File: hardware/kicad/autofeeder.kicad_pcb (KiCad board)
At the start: 4 copper layers, 56 x 54 mm, 44 parts, among them J1 JST_XH_B2B-XH-A_1x02_P2.50mm_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, J3 USB_C_Receptacle_HRO_TYPE-C-3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, J4 PinHeader_1x04_P2.54mm_Vertic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, SW1_POWER1 SW_Push_1P1T_NO_CK_KMR2, SW2_TIMER1 SW_Push_1P1T_NO_CK_KMR2, SW3_MANUAL1 SW_Push_1P1T_NO_CK_KMR2, SW4_SETTINGS1 SW_Push_1P1T_NO_CK_KMR2, SW5_UP1 SW_Push_1P1T_NO_CK_KMR2, SW6_DOWN1 SW_Push_1P1T_NO_CK_KMR2, U1 ESP32_C6_Zero, U2 SOIC-8_3.9x4.9mm_P1.27mm, U3 SOT-23-6_Handsoldering, U4 WSON-10-1EP_2.5x2.5mm_P0.5mm_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, U6 SOIC-8_3.9x4.9mm_P1.27mm, U8 SOT-23-6_Handsoldering

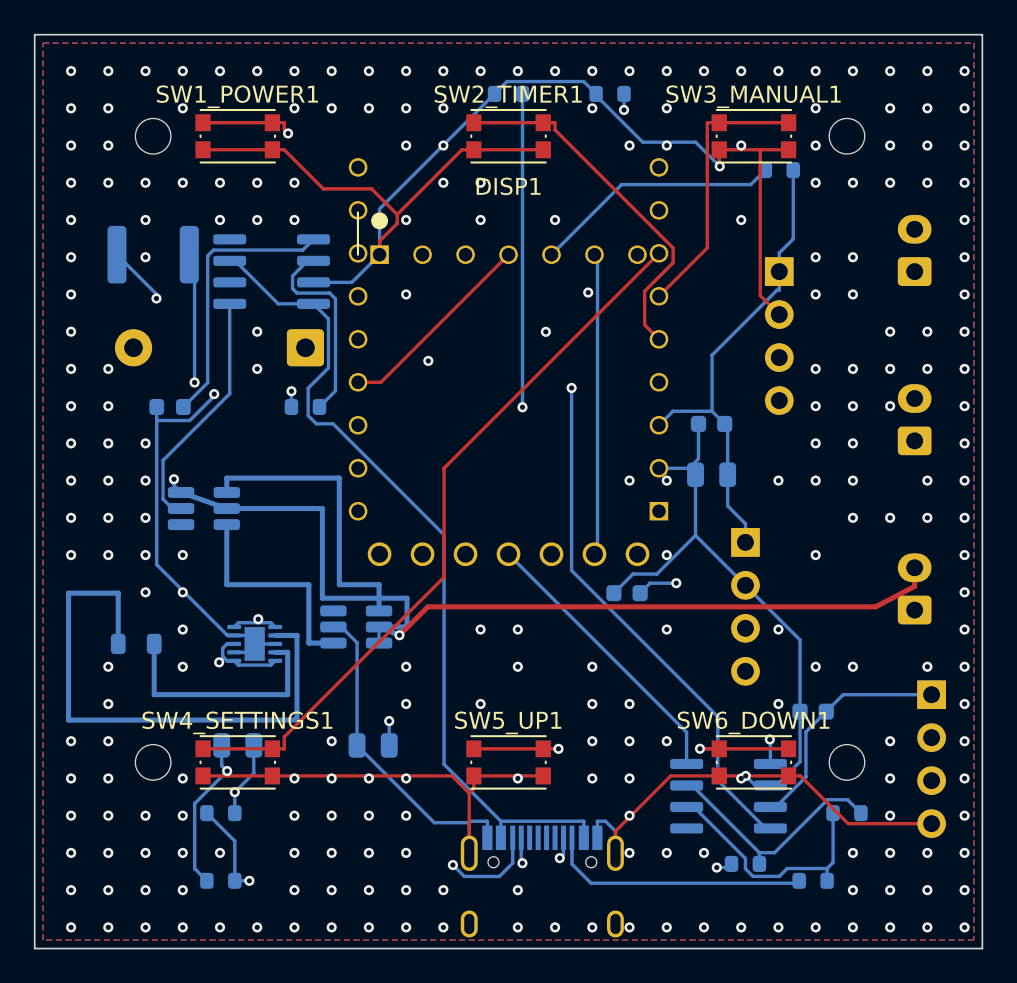
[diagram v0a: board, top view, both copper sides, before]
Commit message: Fix three real shorts in BATT_N pre-routes (battery short + gate crossing)
Commit 04d4fbc shipped 3 DRC error-level violations mislabeled as "marginal
clearance". They were real shorts, all in _pre_route_batt_n():

  1. BATT_N F.Cu track grazed J1 pad 1 (BATT_P) -> dead short across the battery.
  2. OD_GATE (x=20.35 vert) and BATT_N (y=33.3 horiz) crossed on B.Cu at
     (20.35,33.3) -> gate/BATT_N short.
  3. Solder-mask bridge at the same spot as #1.

Fixes:
  - F.Cu J1 exit rerouted left at y=31.5 then down at x=49.69 (left of pad 1's
    x=51 edge), so it never approaches BATT_P.
  - B.Cu U3->U8-2 chain keeps the high y=33.3 path but hops OVER the OD_GATE
    vertical on F.Cu (x19.5->21.2) with two through-vias. Keeping BATT_N high
    preserves the GND pour flow through the U8 inter-column gap that feeds the
    U8-5 GND pocket (a first attempt routing BATT_N down that gap isolated the
    pocket into an unconnected GND island).

Verified (kicad-cli pcb drc --severity-all --schematic-parity): 0 unconnected,
0 error-level violations, B.Cu GND is a single connected plane. Remaining: 11
cosmetic silk warnings + 95 pre-existing schematic-parity items. Fab outputs
(gerbers, drill, DRC) regenerated.

Co-Authored-By: Claude Opus 4.8 <noreply@anthropic.com>
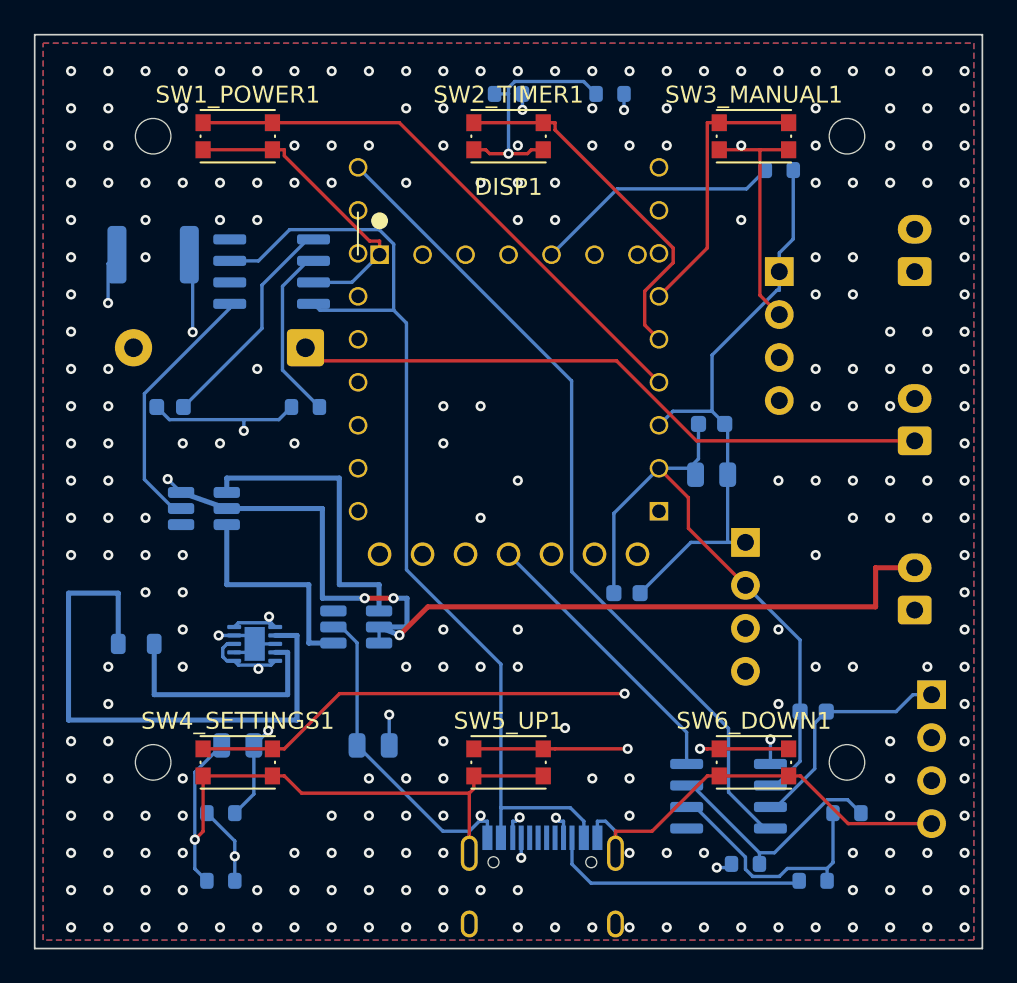
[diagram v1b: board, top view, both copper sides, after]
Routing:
- net GND: track 276.9 -> 298.7 mm, vias 249 -> 243
- net /BATT_PROT: track 101.4 -> 88.7 mm
- net /BUTTON_SETTINGS: track 43.3 -> 53.3 mm, vias 0 -> 1
- net /VBUS: track 49.6 -> 59.6 mm
- net /CC2: track 55.9 -> 46.8 mm
- net /CAN_RX: track 56.4 -> 49.4 mm, vias 1 -> 0
- net /BUTTON_DOWN: track 46.2 -> 40.6 mm
- net /CAN_TX: track 49.3 -> 52.5 mm
- net /CHRG_L: track 16.2 -> 13.3 mm
- net /DISP_MOSI: track 12.0 -> 14.8 mm
- net /CC1: track 47.8 -> 50.5 mm
- net /BUTTON_UP: track 44.8 -> 42.4 mm
- net /BAT_MON: track 28.0 -> 26.1 mm
- net /PROG: track 11.9 -> 10.5 mm
- net /MOTOR_IN2: track 40.0 -> 38.7 mm, vias 1 -> 0
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
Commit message: Set footprint Value + full FPID in populate() (schematic parity)
populate() only called SetReference(), so every footprint kept the library's
default Value (the footprint name, e.g. C1 showed "C_0603_1608Metric" instead of
"100nF") and a bare FPID without its library nickname. That made all 39 components
fail schematic-parity on the value and footprint fields (78 mismatches) and made
the PCB unreadable, even though the copper/nets were correct.

Now carry the schematic value (_value_name from the netlist) via SetValue() and
the full lib:name FPID via SetFPIDAsString(). Schematic parity drops 95 -> 17;
the remaining 17 are out of scope (12 = 4-pin switch symbol vs 2-pad KMR2
footprint, buttons work; 5 = mounting holes + logo not in the schematic). Board
stays 0 unconnected / 0 DRC error-level violations. Three new benign warnings:
'autofeeder' lib not in the project fp-lib-table (footprints are embedded) and
J3's intentional dropped silk differing from the stock USB-C library footprint.

Co-Authored-By: Claude Opus 4.8 <noreply@anthropic.com>
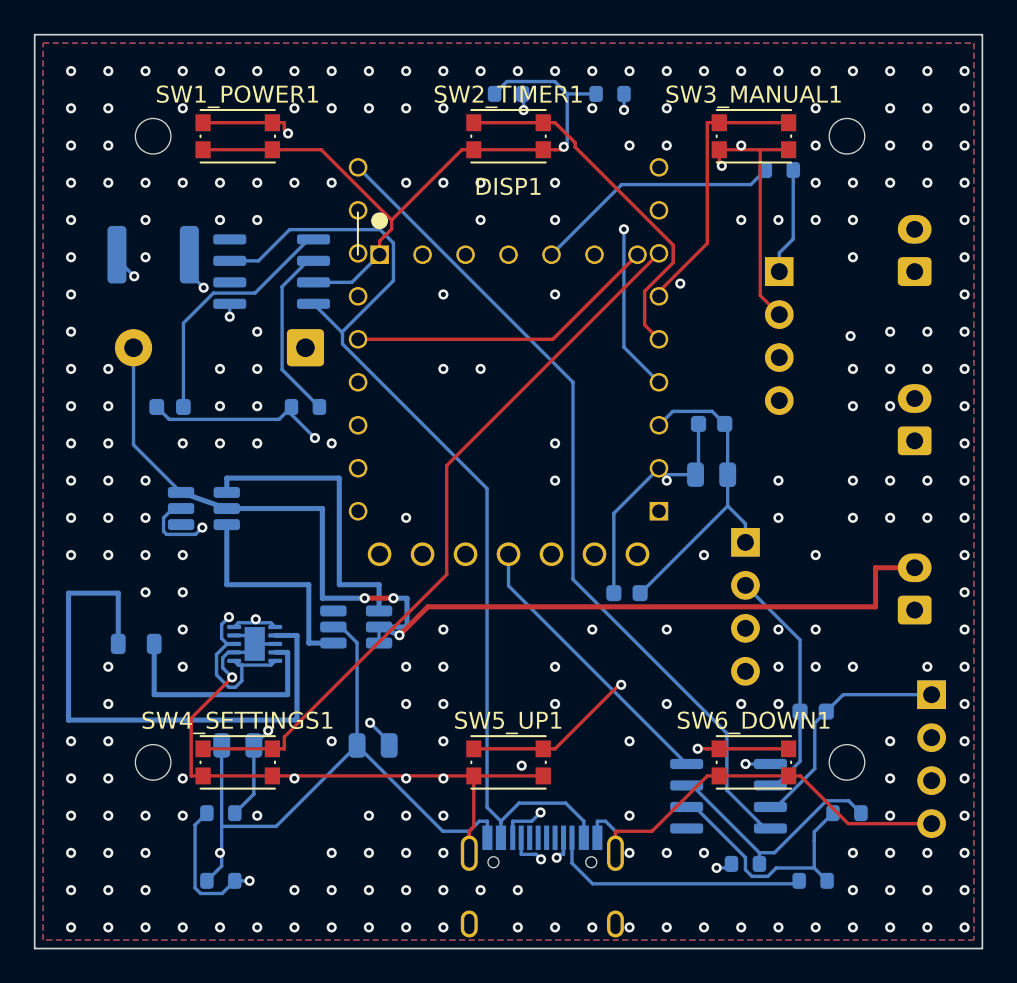
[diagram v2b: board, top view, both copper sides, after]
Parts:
- C1, C3, C6: value C_0603_1608Metric -> 100nF; footprint C_0603_1608Metric -> Capacitor_SMD:C_0603_1608Metric
- C2, C4: value C_0805_2012Metric -> 10uF; footprint C_0805_2012Metric -> Capacitor_SMD:C_0805_2012Metric
- C5: value C_0805_2012Metric -> 22uF; footprint C_0805_2012Metric -> Capacitor_SMD:C_0805_2012Metric
- D1: value D_DO-41_SOD81_P10.16mm_Horizontal -> 1N5817; footprint D_DO-41_SOD81_P10.16mm_Horizontal -> Diode_THT:D_DO-41_SOD81_P10.16mm_Horizontal
- DISP1: value OLED_1.3in_SSD1306_SPI -> OLED_SSD1306; footprint OLED_1.3in_SSD1306_SPI -> autofeeder:OLED_1.3in_SSD1306_SPI
- F1: value Fuse_1812_4532Metric -> 500mA; footprint Fuse_1812_4532Metric -> Fuse:Fuse_1812_4532Metric
- J1: value JST_XH_B2B-XH-A_1x02_P2.50mm_Vertical -> BATTERY; footprint JST_XH_B2B-XH-A_1x02_P2.50mm_Vertical -> Connector_JST:JST_XH_B2B-XH-A_1x02_P2.50mm_Vertical
- J3: value USB_C_Receptacle_HRO_TYPE-C-31-M-12 -> USB-C; footprint USB_C_Receptacle_HRO_TYPE-C-31-M-12 -> Connector_USB:USB_C_Receptacle_HRO_TYPE-C-31-M-12
- J4: value PinHeader_1x04_P2.54mm_Vertical -> DBG; footprint PinHeader_1x04_P2.54mm_Vertical -> Connector_PinHeader_2.54mm:PinHeader_1x04_P2.54mm_Vertical
- J_GPS1: value PinHeader_1x04_P2.54mm_Vertical -> GPS; footprint PinHeader_1x04_P2.54mm_Vertical -> Connector_PinHeader_2.54mm:PinHeader_1x04_P2.54mm_Vertical
- J_MOTOR_CTRL1: value JST_XH_B2B-XH-A_1x02_P2.50mm_Vertical -> MOTOR_CTRL; footprint JST_XH_B2B-XH-A_1x02_P2.50mm_Vertical -> Connector_JST:JST_XH_B2B-XH-A_1x02_P2.50mm_Vertical
- J_MOTOR_PWR1: value JST_XH_B2B-XH-A_1x02_P2.50mm_Vertical -> MOTOR_PWR; footprint JST_XH_B2B-XH-A_1x02_P2.50mm_Vertical -> Connector_JST:JST_XH_B2B-XH-A_1x02_P2.50mm_Vertical
- J_RTC1: value PinHeader_1x04_P2.54mm_Vertical -> DS3231; footprint PinHeader_1x04_P2.54mm_Vertical -> Connector_PinHeader_2.54mm:PinHeader_1x04_P2.54mm_Vertical
- L1: value L_0805_2012Metric -> 4.7uH; footprint L_0805_2012Metric -> Inductor_SMD:L_0805_2012Metric
- LED_CHG1: value LED_0603_1608Metric -> RED; footprint LED_0603_1608Metric -> LED_SMD:LED_0603_1608Metric
- R10, R6: value R_0603_1608Metric -> 1k; footprint R_0603_1608Metric -> Resistor_SMD:R_0603_1608Metric
- R13: value R_0603_1608Metric -> 10k; footprint R_0603_1608Metric -> Resistor_SMD:R_0603_1608Metric
- R2_C1: value R_0603_1608Metric -> 1.2k; footprint R_0603_1608Metric -> Resistor_SMD:R_0603_1608Metric
- R3, R4: value R_0603_1608Metric -> 47k; footprint R_0603_1608Metric -> Resistor_SMD:R_0603_1608Metric
- R5: value R_0603_1608Metric -> 120R; footprint R_0603_1608Metric -> Resistor_SMD:R_0603_1608Metric
- R_CC1, R_CC2: value R_0603_1608Metric -> 5.1k; footprint R_0603_1608Metric -> Resistor_SMD:R_0603_1608Metric
- SW1_POWER1, SW2_TIMER1, SW3_MANUAL1, SW4_SETTINGS1, SW5_UP1, SW6_DOWN1: value SW_Push_1P1T_NO_CK_KMR2 -> Alps SKRPADE010; footprint SW_Push_1P1T_NO_CK_KMR2 -> Button_Switch_SMD:SW_Push_1P1T_NO_CK_KMR2
- U1: value ESP32_C6_Zero -> ESP32-C6-Zero; footprint ESP32_C6_Zero -> autofeeder:ESP32_C6_Zero
- U2: value SOIC-8_3.9x4.9mm_P1.27mm -> TP4056; footprint SOIC-8_3.9x4.9mm_P1.27mm -> Package_SO:SOIC-8_3.9x4.9mm_P1.27mm
- U3: value SOT-23-6_Handsoldering -> DW01A; footprint SOT-23-6_Handsoldering -> Package_TO_SOT_SMD:SOT-23-6_Handsoldering
- U4: value WSON-10-1EP_2.5x2.5mm_P0.5mm_EP1.2x2mm -> TPS63031DSKR; footprint WSON-10-1EP_2.5x2.5mm_P0.5mm_EP1.2x2mm -> Package_SON:WSON-10-1EP_2.5x2.5mm_P0.5mm_EP1.2x2mm
- U6: value SOIC-8_3.9x4.9mm_P1.27mm -> SN65HVD230; footprint SOIC-8_3.9x4.9mm_P1.27mm -> Package_SO:SOIC-8_3.9x4.9mm_P1.27mm
- U8: value SOT-23-6_Handsoldering -> FS8205A; footprint SOT-23-6_Handsoldering -> Package_TO_SOT_SMD:SOT-23-6_Handsoldering
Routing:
- net /BATT_PROT: track 88.7 -> 99.9 mm
- net /BUTTON_SETTINGS: track 53.3 -> 43.3 mm, vias 1 -> 0
- net GND: track 298.7 -> 292.1 mm, vias 243 -> 251
- net /BATT_P: track 57.9 -> 64.3 mm, vias 1 -> 2
- net /BAT_MON: track 26.1 -> 30.9 mm
- net /BUTTON_POWER: track 33.3 -> 37.6 mm, vias 0 -> 2
- net /VCC_3V3: track 132.3 -> 128.4 mm
- net /BUTTON_UP: track 42.4 -> 39.2 mm
- net /BATT_CHG: track 15.3 -> 18.5 mm, vias 0 -> 2
- net /DISP_SCK: track 12.7 -> 15.6 mm
- net /DISP_MOSI: track 14.8 -> 12.0 mm
- net /CAN_TX: track 52.5 -> 54.6 mm
- net /BUTTON_DOWN: track 40.6 -> 42.1 mm
- net /CC1: track 50.5 -> 49.0 mm
- net /CHRG_L: track 13.3 -> 14.7 mm
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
